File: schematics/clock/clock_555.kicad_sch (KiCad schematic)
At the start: 5 parts, among them U3 74LS08, U4 74LS04, U5 74LS32

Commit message: add change mode case
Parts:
- RLED: renamed from R3; value R -> 469
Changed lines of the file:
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@@
 		(dnp no)
 		(fields_autoplaced yes)
-		(property "Reference" "R3"
+		(property "Reference" "RLED"
 			(at 194.31 129.5399 0)
 			(effects
@@
 			)
 		)
-		(property "Value" "R"
+		(property "Value" "469"
 			(at 194.31 132.0799 0)
 			(effects
@@
 			(project ""
 				(path "/1be175cd-1437-4d72-8152-541f02e1a99b/a2ab6e87-bee2-42a5-8573-76b69ae33327"
-					(reference "R3")
+					(reference "RLED")
 					(unit 1)
 				)

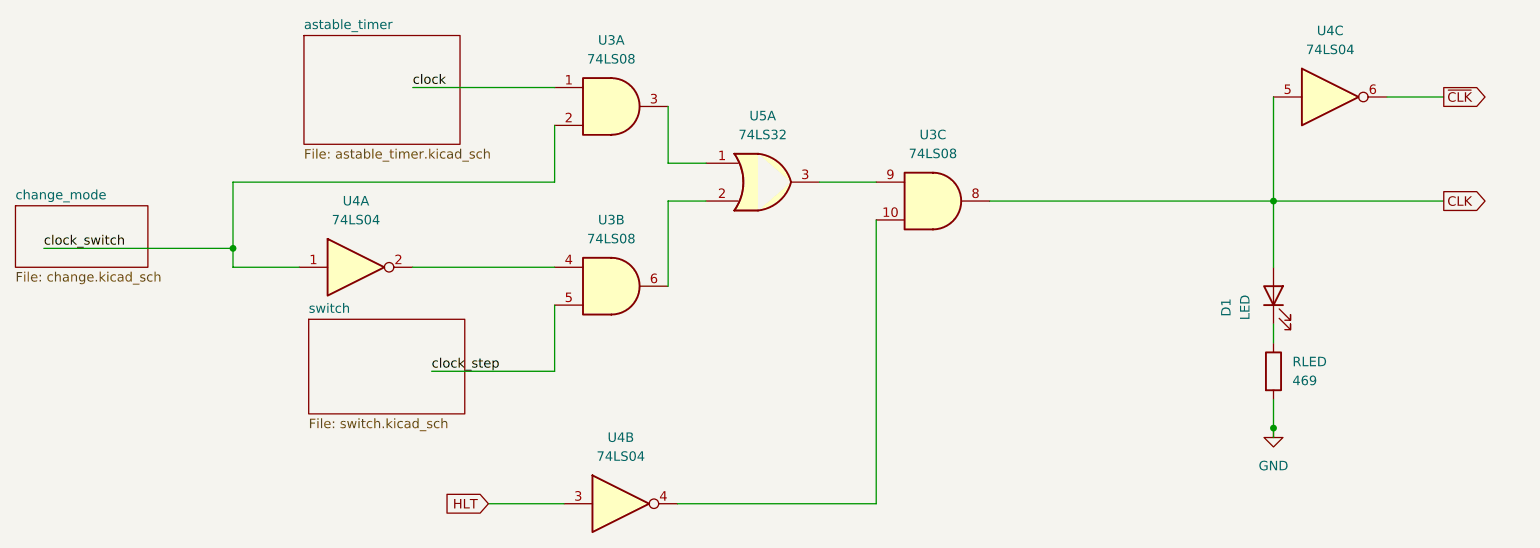
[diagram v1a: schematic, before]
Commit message: apply demorgan to clock
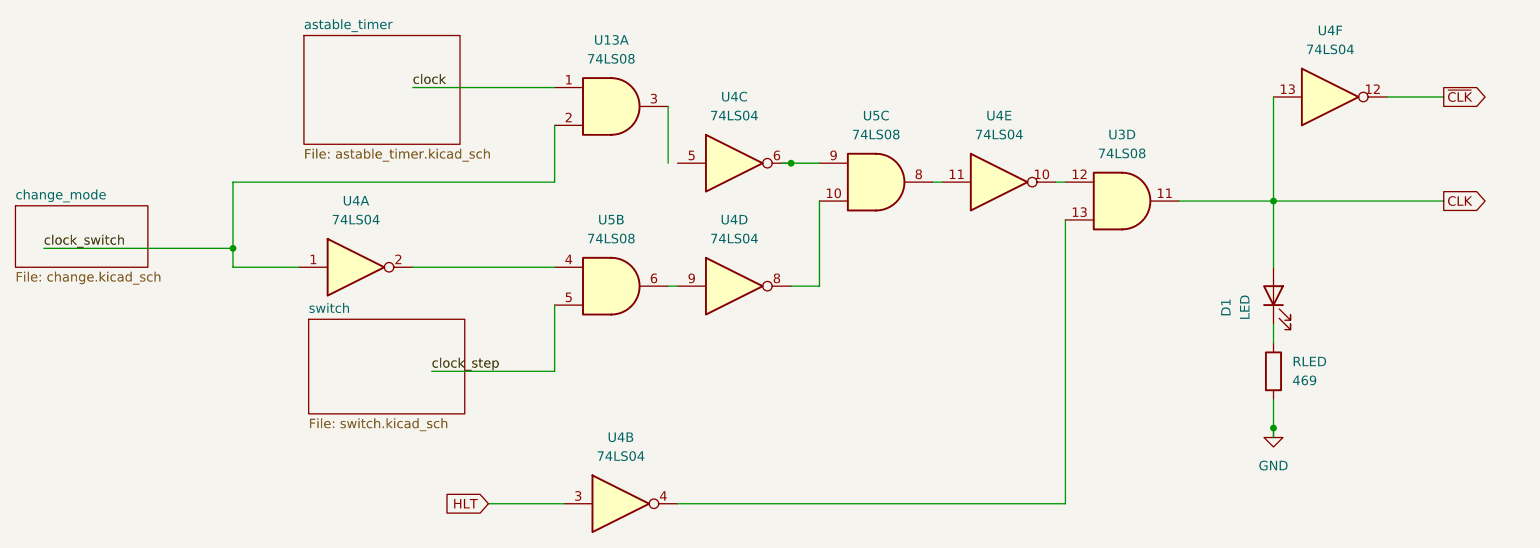
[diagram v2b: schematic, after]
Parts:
- removed U3: 74LS08, symbol 74xx:74LS08
- removed U5: 74LS32, symbol 74xx:74LS32
- added U13, U3, U5: 74LS08, symbol 74xx:74LS08
- added unit 4 of U4
- added unit 5 of U4
- added unit 6 of U4
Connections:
- net CLK: now also U3.11, U4.13; no longer U4.5
- net clock: now also U13.1
- net clock_step: now also U5.5
- net clock_switch: now also U13.2
- net ~{CLK}: now also U4.12; no longer U4.6
- net at U4.4: now also U3.13
- net at U4.2: now also U5.4
- new net: U4.8, U5.10
- new net: U4.9, U5.6
- new net: U3.12, U4.10
- new net: U4.11, U5.8
- new net: U4.6, U5.9
